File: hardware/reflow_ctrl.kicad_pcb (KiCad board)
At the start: 2 copper layers, 21 parts, among them IC1 MAX6675, U2 MOC3063, U3 BTA41/600B, X1 Master, X2 Mains, X3 Load, X4 Thermocouple

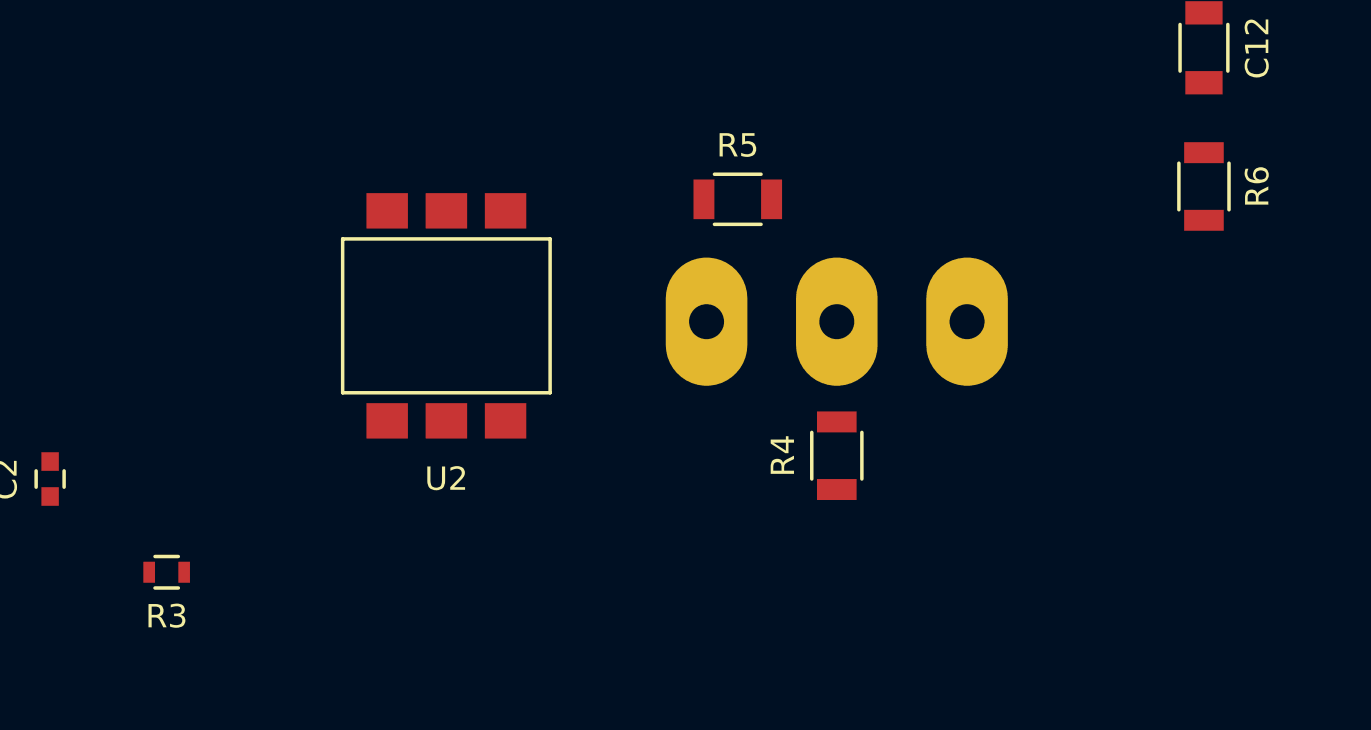
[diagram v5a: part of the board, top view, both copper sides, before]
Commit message: Add and use uMIDI.pretty generic smd packages
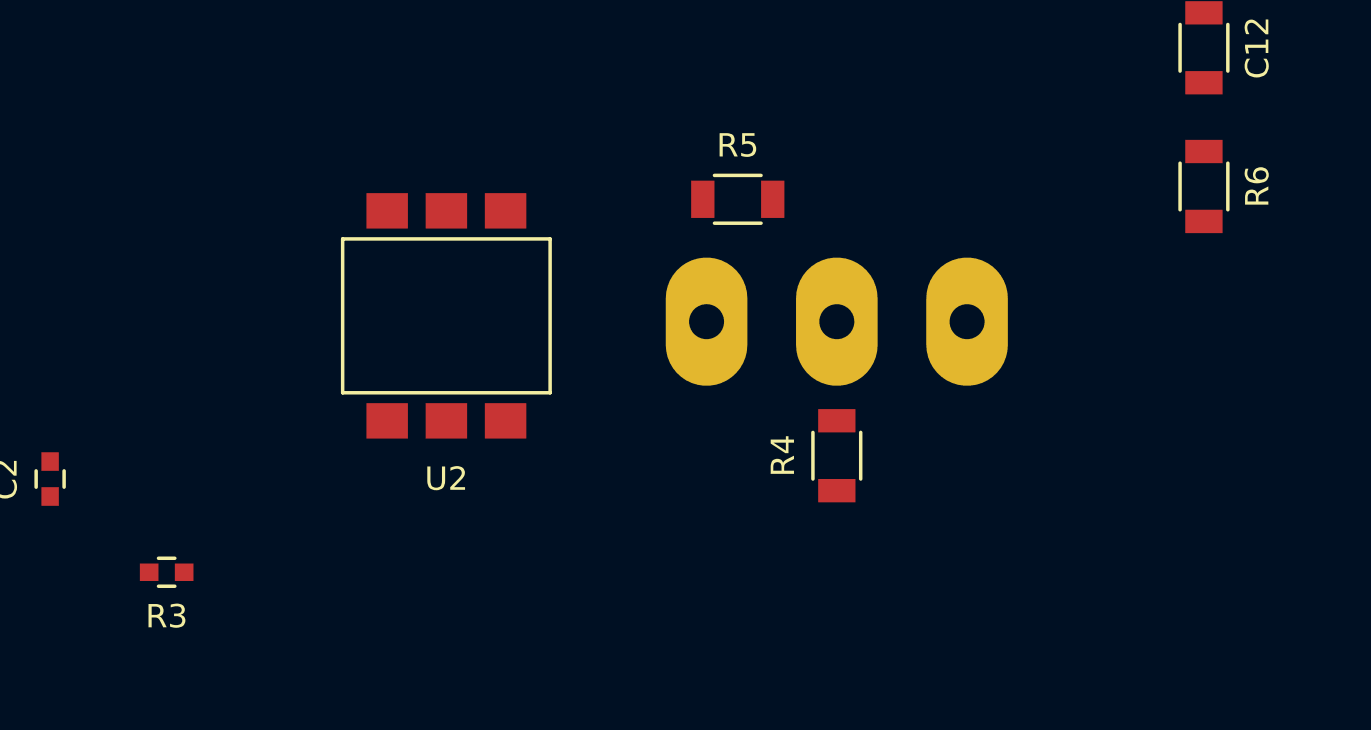
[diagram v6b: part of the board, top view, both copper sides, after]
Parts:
- C1, C11, C2: footprint Capacitors_SMD:C_0603 -> uMIDI:Pas_0603
- C12: footprint Capacitors_SMD:C_1206 -> uMIDI:Pas_1206
- R3: footprint Resistors_SMD:R_0603 -> uMIDI:Pas_0603
- R4, R5, R6: footprint Resistors_SMD:R_1206 -> uMIDI:Pas_1206

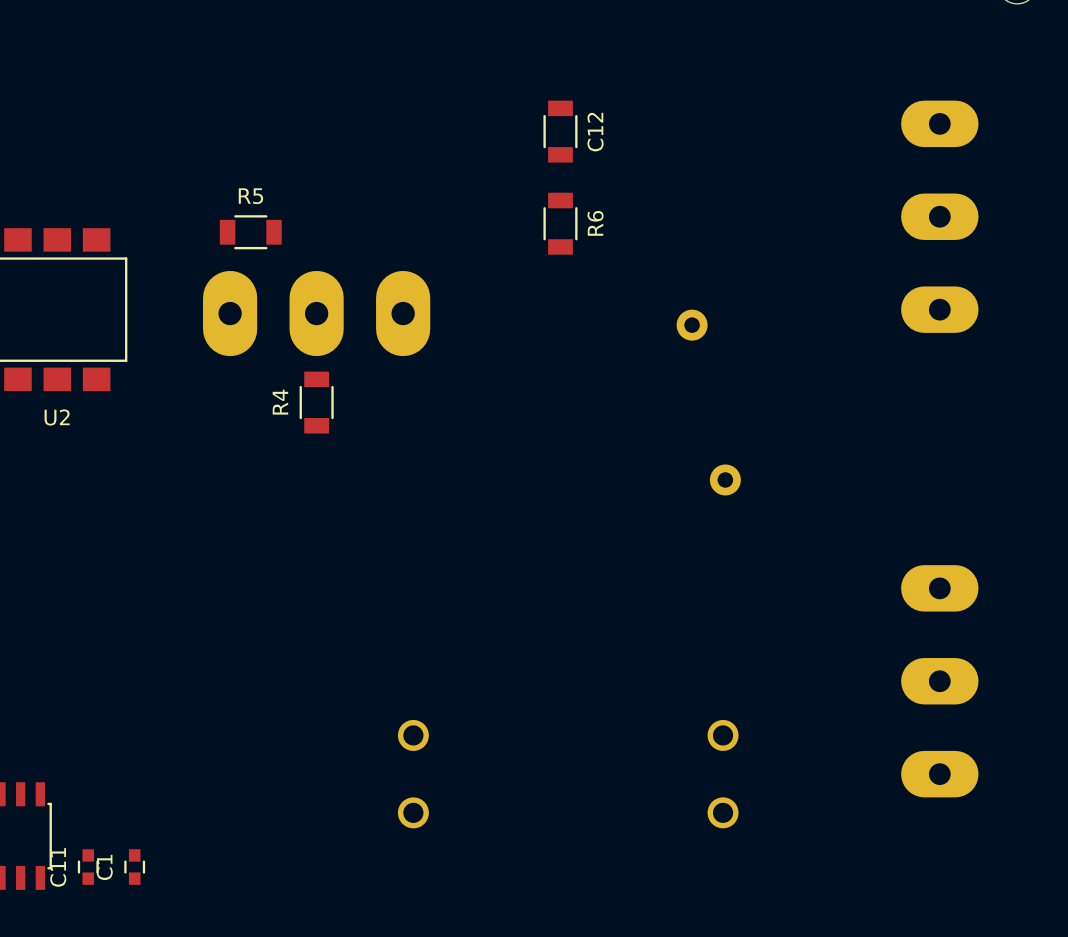
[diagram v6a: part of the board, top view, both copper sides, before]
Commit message: Place and lock heatsink and triac
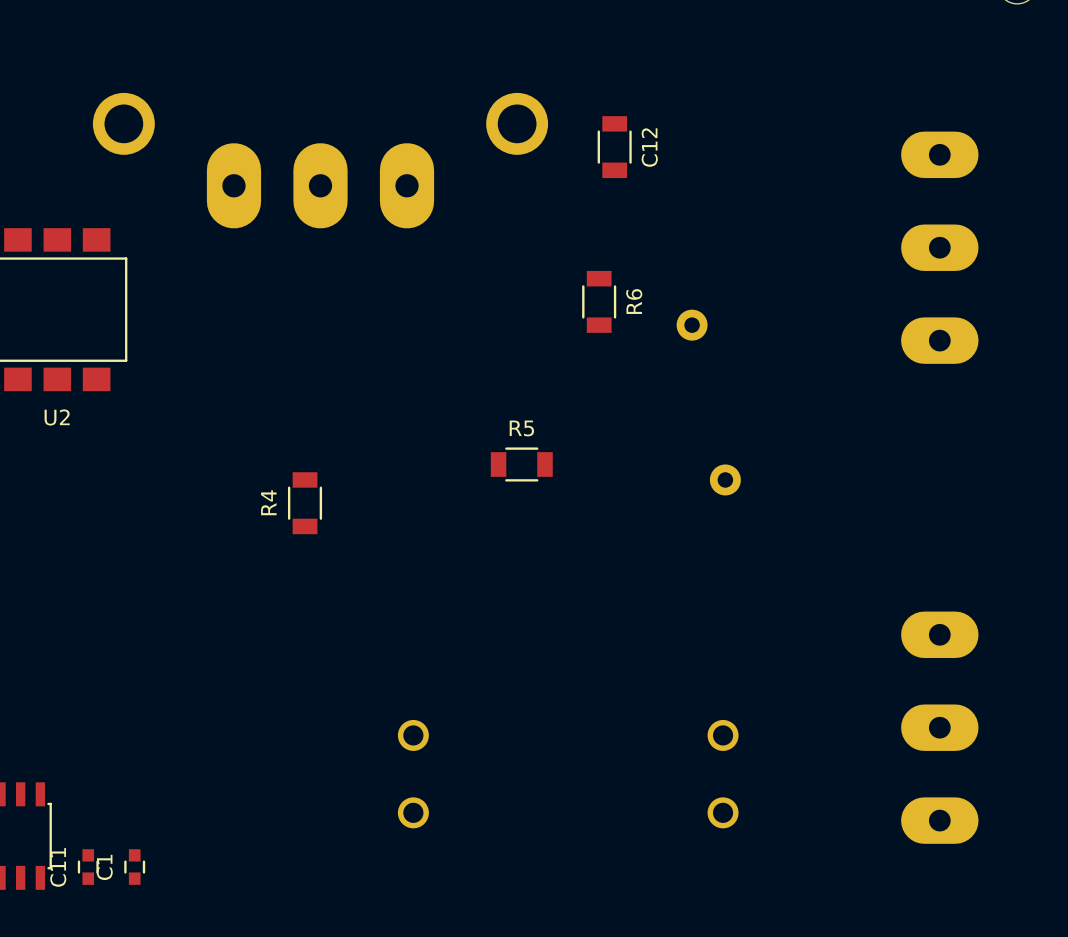
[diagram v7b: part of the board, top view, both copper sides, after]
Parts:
- added HS1: HEATSINK, uMIDI:Mech-Heatsink_Fischer_SK129_STS, B.Cu at (150.0, 64.0)
- moved R5 23.0 mm to (163.0, 86.0)
- moved U3 8.25 mm to (150.0, 68.0), turned to 0 degrees
- moved R4 6.54 mm to (149.0, 88.5)
- moved R6 5.63 mm to (168.0, 75.5)
- moved C12 3.64 mm to (169.0, 65.5)
- moved X2 3.00 mm to (190.0, 103.0)
- moved X3 2.00 mm to (190.0, 72.0)
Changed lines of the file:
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@@
     (links 33)
     (no_connects 33)
-    (area 0 0 0 0)
+    (area 95.615476 49.075 213 132.700001)
     (thickness 1.6)
     (drawings 6)
     (tracks 0)
     (zones 0)
-    (modules 21)
+    (modules 22)
     (nets 18)
   )
@@
       (net 16 /MOC_A2))
   )
-  (module TO_SOT_Packages_THT:TO-247_Vertical_Neutral123_largePads (layer B.Cu)
-    (at 149.75 76.25 180)
+  (module TO_SOT_Packages_THT:TO-247_Vertical_Neutral123_largePads locked (layer B.Cu)
+    (at 150 68)
     (descr "TO-247 TO-218 TOP-3 FET 1=Gate 2=Drain 3=Source Vertical, large Pads")
     (tags "Transistor FET TO-247 TO-218 TOP-3 Vertical")
-    (fp_text reference U3 (at 0 5.08 180) (layer B.SilkS)
-      (effects (font (size 1 1) (thickness 0.15)) (justify mirror))
-    )
-    (fp_text value BTA41/600B (at -1.016 -8.128 180) (layer B.Fab)
+    (fp_text reference U3 (at 0 5.08) (layer B.SilkS)
+      (effects (font (size 1 1) (thickness 0.15)) (justify mirror))
+    )
+    (fp_text value BTA41/600B (at -1.016 -8.128) (layer B.Fab)
       (effects (font (size 1 1) (thickness 0.15)) (justify mirror))
     )
@@
     (fp_line (start 8.128 -2.794) (end 8.128 2.794) (layer B.SilkS) (width 0.15))
     (fp_line (start -8.128 2.794) (end -8.128 -2.794) (layer B.SilkS) (width 0.15))
-    (pad 2 thru_hole oval (at 0 0 90) (size 5.50164 3.50012) (drill 1.50114) (layers *.Cu *.Mask B.SilkS)
+    (pad 2 thru_hole oval (at 0 0 270) (size 5.50164 3.50012) (drill 1.50114) (layers *.Cu *.Mask B.SilkS)
       (net 17 /L_main_fused))
-    (pad 1 thru_hole oval (at -5.588 0 90) (size 5.50164 3.50012) (drill 1.50114) (layers *.Cu *.Mask B.SilkS)
+    (pad 1 thru_hole oval (at -5.588 0 270) (size 5.50164 3.50012) (drill 1.50114) (layers *.Cu *.Mask B.SilkS)
       (net 3 /L_load))
-    (pad 3 thru_hole oval (at 5.588 0 90) (size 5.50164 3.50012) (drill 1.50114) (layers *.Cu *.Mask B.SilkS)
+    (pad 3 thru_hole oval (at 5.588 0 270) (size 5.50164 3.50012) (drill 1.50114) (layers *.Cu *.Mask B.SilkS)
       (net 16 /MOC_A2))
   )
@@
   )
   (module uMIDI:Mains_Solder (layer B.Cu)
-    (at 190 100 90)
+    (at 190 103 90)
     (descr "3 terminals for soldering to a 1,5mm^2 cord")
     (tags "Mains AC 1,5mm^2")
@@
   )
   (module uMIDI:Mains_Solder (layer B.Cu)
-    (at 190 70 270)
+    (at 190 72 270)
     (descr "3 terminals for soldering to a 1,5mm^2 cord")
     (tags "Mains AC 1,5mm^2")
@@
   )
   (module uMIDI:Pas_1206 (layer F.Cu)
-    (at 165.5 64.5 270)
+    (at 169 65.5 270)
     (descr "Generic SMD 1206 package")
     (tags 1206)
@@
   )
   (module uMIDI:Pas_1206 (layer F.Cu)
-    (at 149.75 82 90)
+    (at 149 88.5 90)
     (descr "Generic SMD 1206 package")
     (tags 1206)
@@
   )
   (module uMIDI:Pas_1206 (layer F.Cu)
-    (at 145.5 71)
+    (at 163 86)
     (descr "Generic SMD 1206 package")
     (tags 1206)
@@
   )
   (module uMIDI:Pas_1206 (layer F.Cu)
-    (at 165.5 70.45 270)
+    (at 168 75.5 270)
     (descr "Generic SMD 1206 package")
     (tags 1206)
@@
     )
   )
+  (module uMIDI:Mech-Heatsink_Fischer_SK129_STS locked (layer B.Cu)
+    (at 150 64)
+    (fp_text reference HS1 (at -18.5 11.5) (layer B.SilkS)
+      (effects (font (size 1 1) (thickness 0.15)) (justify mirror))
+    )
+    (fp_text value HEATSINK (at 22.5 0 270) (layer B.Fab)
+      (effects (font (size 1 1) (thickness 0.15)) (justify mirror))
+    )
+    (fp_line (start -1.6 0.9) (end -1.6 0.7) (layer B.SilkS) (width 0.15))
+    (fp_line (start -21 12.5) (end -21 -12.5) (layer B.SilkS) (width 0.15))
+    (fp_line (start -8.5 -12.5) (end -21 -12.5) (layer B.SilkS) (width 0.15))
+    (fp_line (start -8.5 -12.5) (end -8.5 -0.9) (layer B.SilkS) (width 0.15))
+    (fp_line (start 8.5 -0.9) (end -8.5 -0.9) (layer B.SilkS) (width 0.15))
+    (fp_line (start 8.5 0.9) (end -8.5 0.9) (layer B.SilkS) (width 0.15))
+    (fp_line (start 21 -12.5) (end 8.5 -12.5) (layer B.SilkS) (width 0.15))
+    (fp_line (start 8.5 -12.5) (end 8.5 -0.9) (layer B.SilkS) (width 0.15))
+    (fp_line (start -8.5 0.9) (end -8.5 12.5) (layer B.SilkS) (width 0.15))
+    (fp_line (start 8.5 0.9) (end 8.5 12.5) (layer B.SilkS) (width 0.15))
+    (fp_line (start -8.5 12.5) (end -21 12.5) (layer B.SilkS) (width 0.15))
+    (fp_line (start 21 12.5) (end 8.5 12.5) (layer B.SilkS) (width 0.15))
+    (fp_line (start 21 12.5) (end 21 -12.5) (layer B.SilkS) (width 0.15))
+    (fp_line (start -1.6 0.4) (end -1.6 0.2) (layer B.SilkS) (width 0.15))
+    (fp_line (start -1.6 -0.7) (end -1.6 -0.9) (layer B.SilkS) (width 0.15))
+    (fp_line (start -1.6 -0.2) (end -1.6 -0.4) (layer B.SilkS) (width 0.15))
+    (fp_line (start 1.6 0.9) (end 1.6 0.7) (layer B.SilkS) (width 0.15))
+    (fp_line (start 1.6 -0.2) (end 1.6 -0.4) (layer B.SilkS) (width 0.15))
+    (fp_line (start 1.6 0.4) (end 1.6 0.2) (layer B.SilkS) (width 0.15))
+    (fp_line (start 1.6 -0.7) (end 1.6 -0.9) (layer B.SilkS) (width 0.15))
+    (pad 1 thru_hole circle (at -12.7 0) (size 4 4) (drill 2.5) (layers *.Cu *.Mask))
+    (pad 1 thru_hole circle (at 12.7 0) (size 4 4) (drill 2.5) (layers *.Cu *.Mask))
+  )
   (dimension 75 (width 0.3) (layer Dwgs.User)

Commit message: Start place and route
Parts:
- moved C12 27.7 mm to (143.0, 75.0), turned to 180 degrees
- moved R5 27.3 mm to (150.0, 62.0), turned to 180 degrees
- moved R6 19.0 mm to (149.0, 75.0), turned to 180 degrees
- moved U2 18.0 mm to (139.0, 93.0), turned to 270 degrees
- moved VR1 14.2 mm to (162.0, 87.0), turned to 0 degrees
- moved F1 5.83 mm to (161.0, 103.0)
- moved R3 4.37 mm to (125.2, 86.0)
- moved R4 1.12 mm to (148.0, 89.0), turned to 270 degrees
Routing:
- net /L_load: track 0.00 -> 90.3 mm
- net /MOC_A2: track 0.00 -> 80.6 mm
- net /L_main_fused: track 0.00 -> 53.8 mm
- net /PE_mains: track 0.00 -> 43.2 mm
- net /N_mains: track 0.00 -> 19.0 mm
- net /Snub: track 0.00 -> 3.00 mm
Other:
- net class AC: trace_width 5 -> 3
